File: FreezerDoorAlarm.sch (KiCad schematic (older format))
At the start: 36 parts, among them J1 Barrel_Jack, J2 Conn_01x02_Female, J3 Conn_01x01, J4 Conn_01x01, Q1 MMBT3906, Q2 MMBT3904, Q3 MMBT3906, Q4 MMBT3904, Q5 BSS138, Q6 MMBT3906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

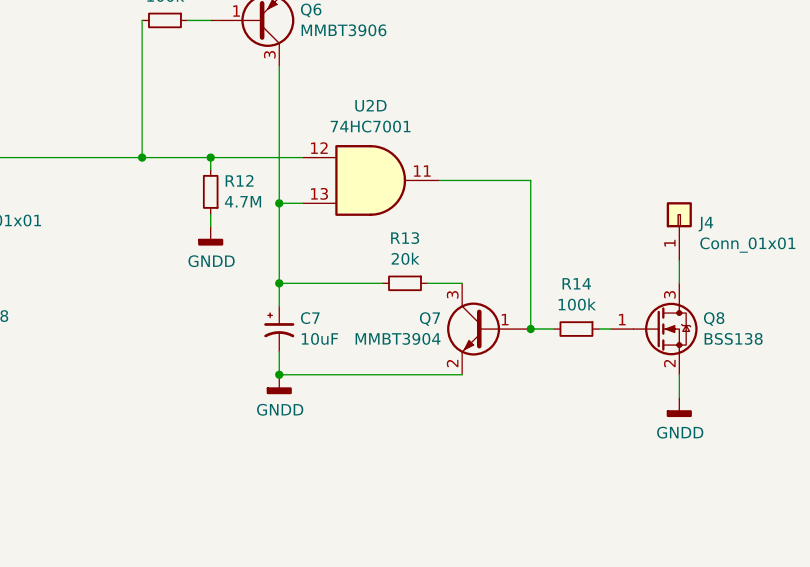
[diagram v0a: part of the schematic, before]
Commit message: Where large/fast currents are expected to flow (Q2/C5, U2 bypass) loop area has been reduced.
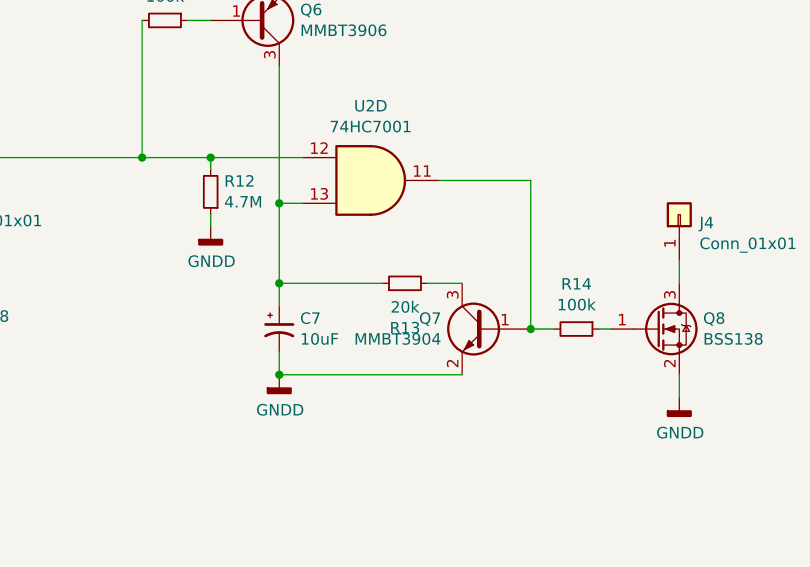
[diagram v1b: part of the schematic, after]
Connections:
- net at C7.1, Q6.3 (C), U2.13: now also R13.1; no longer R13.2
- net at Q7.3 (C): now also R13.2; no longer R13.1
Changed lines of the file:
@@
 F 3 "~" H 9350 4050 50  0001 C CNN
 	1    9350 4050
-	0    1    1    0
+	0    -1   -1   0
 $EndComp
 Wire Wire Line
